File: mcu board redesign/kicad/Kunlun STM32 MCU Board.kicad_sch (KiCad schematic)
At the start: 33 parts, among them J1 0532610671, J2 10129383-908001ALF, J3 USB4105-GF-A, J4 5002, J5 5002, J6 5002, J7 5002, J8 5001, J9 5001, SW1 KMR231NG ULC LFS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

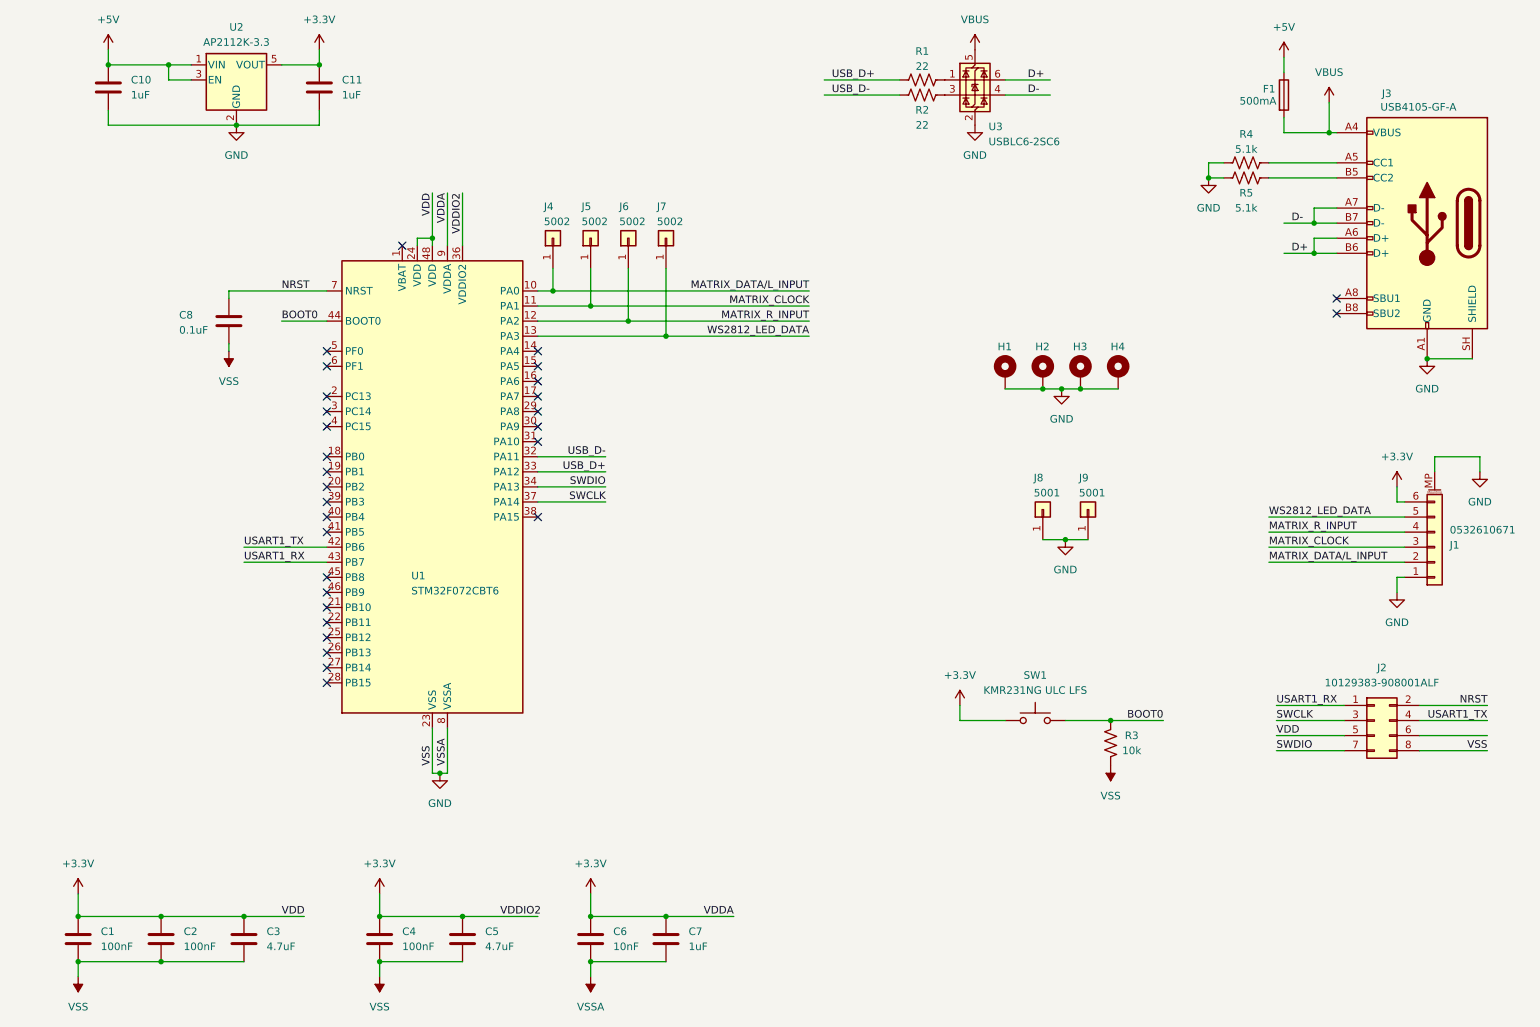
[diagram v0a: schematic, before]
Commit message: Lots of updates
Add ESD protection R6/C9
Layout changes for bypass caps
Layout changes to pass all JLC DFM checks
Fill out J2 and optimize routing
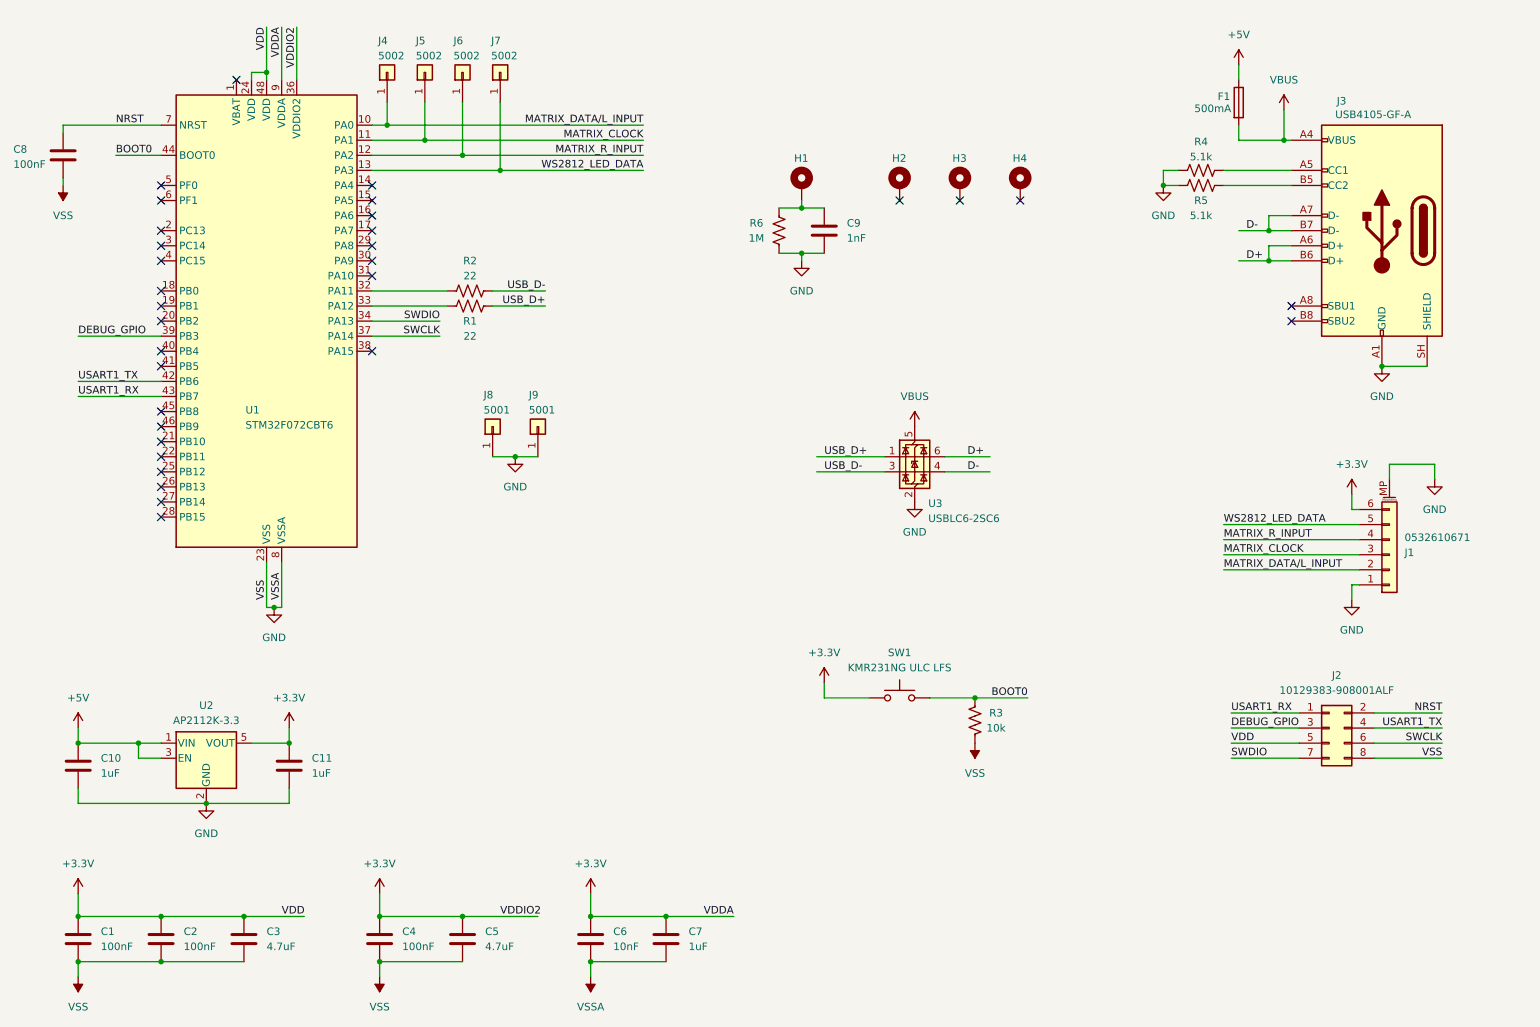
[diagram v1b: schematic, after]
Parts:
- added C9: 1nF, Capacitor_SMD:C_1206_3216Metric, symbol Device:C
- added R6: 1M, Resistor_SMD:R_1206_3216Metric, symbol Device:R_US
- C1, C2, C4: PartNo C0603C104K5RACTU -> 399-C0603C104K5RACTUCT-ND
- C10, C11, C7: PartNo C0603C105K4RACTU -> 399-C0603C105K4RACTUCT-ND
- C3, C5: PartNo (none) -> 399-C0603C475K9PACTUCT-ND
- C6: PartNo C0603C103K5RACTU -> 399-C0603C103K5RACTUCT-ND
- C8: value 0.1uF -> 100nF; PartNo C0603C104K5RACTU -> 399-C0603C104K5RACTUCT-ND
- H1, H2, H3, H4: footprint MountingHole:MountingHole_2.2mm_M2_Pad_Via -> MountingHole:MountingHole_2.2mm_M2_Pad
- J1: PartNo 0532610671 -> WM7624CT-ND
- J2: PartNo 10129383-908001ALF -> 609-10129383-908001ALFCT-ND
- J3: PartNo USB4105-GF-A -> 2073-USB4105-GF-ACT-ND
- J4, J5, J6, J7: PartNo (none) -> 36-5002-ND
- J8, J9: PartNo (none) -> 36-5001-ND
- R1, R2: PartNo RMCF0603FT22R0 -> RMCF0603FT22R0CT-ND
- R3: PartNo RMCF0603JT10K0 -> RMCF0603JT10K0CT-ND
- R4, R5: PartNo RC0603FR-075K1L -> RMCF0603FT5K10CT-ND
- SW1: PartNo KMR231NG ULC LFS -> CKN10284CT-ND
- U1: PartNo (none) -> 497-14645-ND
- U2: PartNo AP2112K-3.3 -> AP2112K-3.3TRG1DICT-ND
- U3: PartNo USBLC6-2SC6 -> 497-5235-1-ND
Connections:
- net GND: now also C9.2, R6.2; no longer H1.1, H2.1, H3.1, H4.1
- net SWCLK: now also J2.6 (Pin_6); no longer J2.3 (Pin_3)
- net USB_D+: now also R1.1, U3.1 (I/O1); no longer R1.2, U1.33 (PA12)
- net USB_D-: now also R2.1, U3.3 (I/O2); no longer R2.2, U1.32 (PA11)
- net DEBUG_GPIO: now reaches U1.39 (PB3)
- net DEBUG_GPIO: now also J2.3 (Pin_3)
- new net: C9.1, H1.1, R6.1
- new net: R2.2, U1.32 (PA11)
- new net: R1.2, U1.33 (PA12)
- no-connect marks 30 -> 32
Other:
- moved on the sheet: C10, C11, C8, F1, H1, J1, J2, J3, J4, J5, J6, J7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

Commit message: Mostly layout updates
Add VBUS decoupling cap.
Rearrange traces for less ground plane chops and fewer vias.
Move some components around for trace optimization (boot switch, etc)
Tweak the decoupling caps
Remove pads from 3 mounting holes to avoid potential chassis ground loops
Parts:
- removed H2, H3, H4: MountingHole_Pad, MountingHole:MountingHole_2.2mm_M2_Pad, symbol Mechanical:MountingHole_Pad
- added C10: 1uF, Capacitor_SMD:C_0603_1608Metric, symbol Device:C
- renumbered C10 to C11, C11 to C12
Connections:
- net GND: now also C10.2; no longer J1.MP (MountPin)
- net VBUS: now also C10.1
- no-connect marks 32 -> 30
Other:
- moved on the sheet: C1, C2, C3, C4, C5, C6, C7, C9, H1, R6

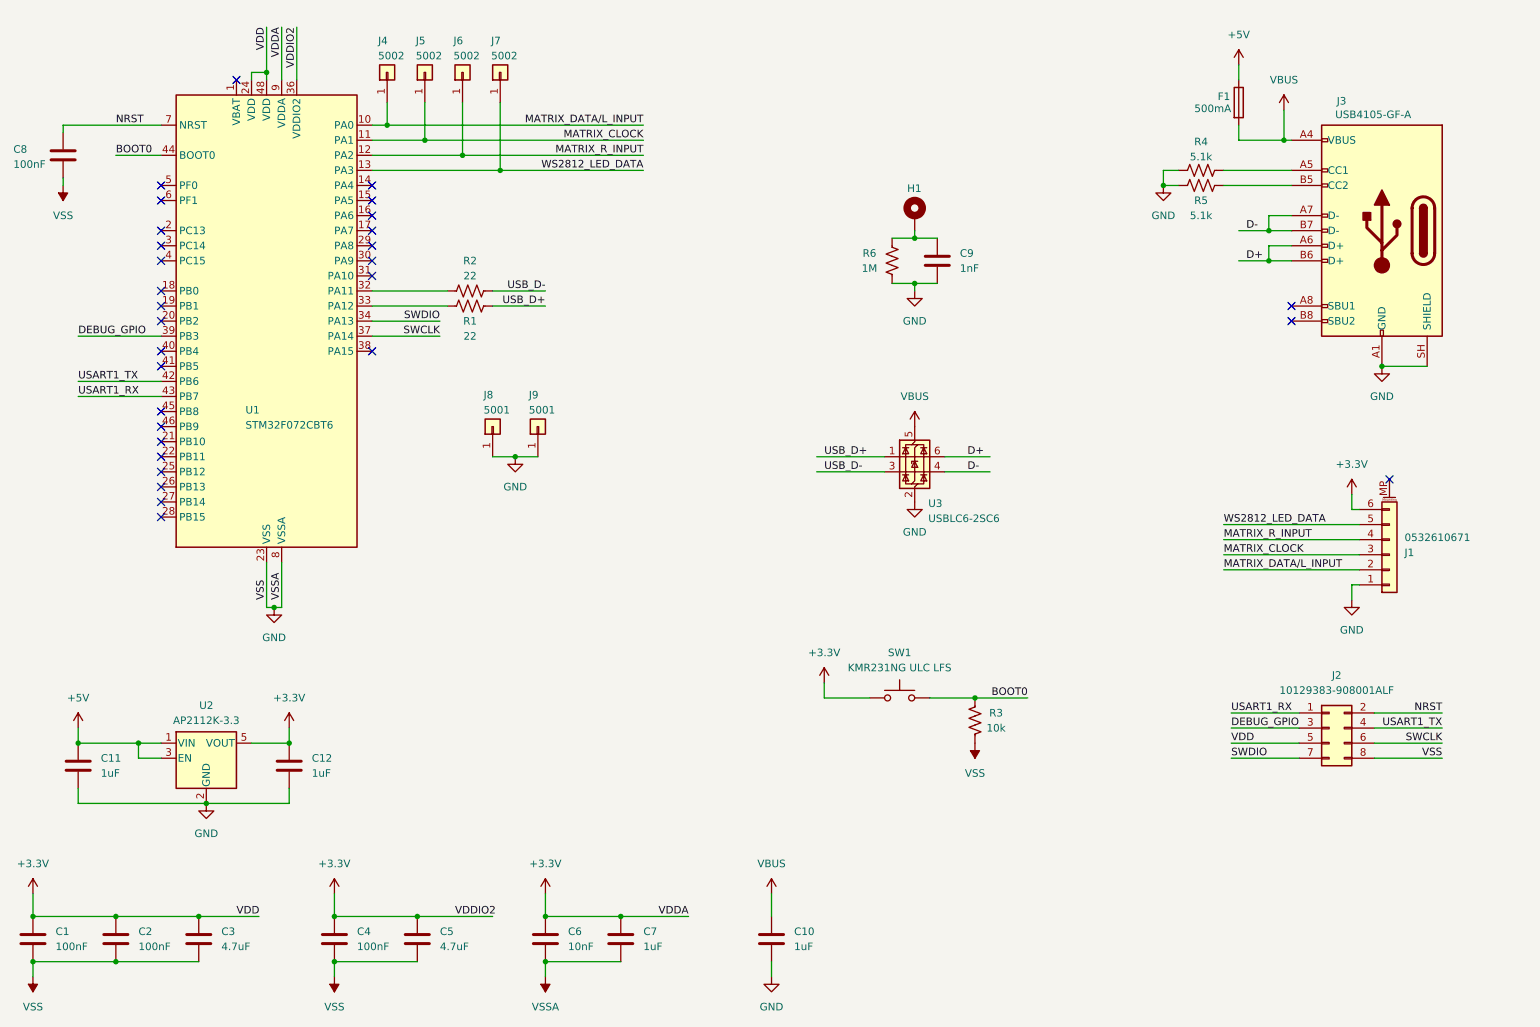
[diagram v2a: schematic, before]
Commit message: Added speaker, changed fuse.
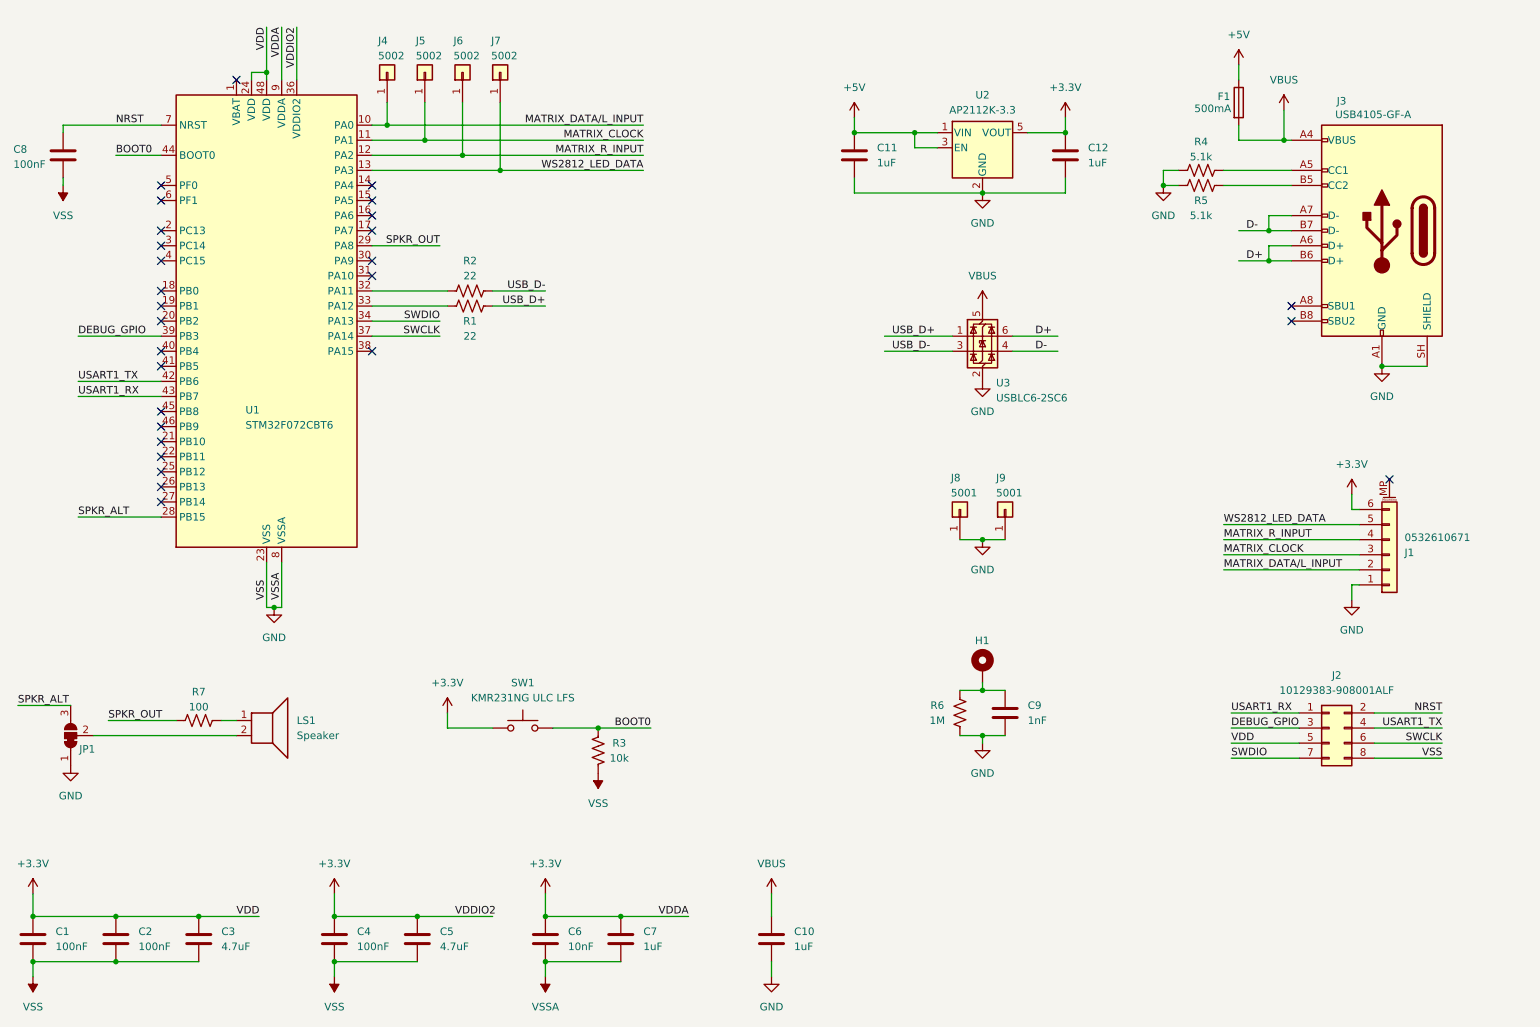
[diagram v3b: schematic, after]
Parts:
- added JP1: SolderJumper_3_Bridged12, Jumper:SolderJumper-3_P1.3mm_Bridged12_RoundedPad1.0x1.5mm, symbol Jumper:SolderJumper_3_Bridged12
- added LS1: Speaker, Buzzer_Beeper:Buzzer_CUI_CPT-9019S-SMT, symbol Device:Speaker
- added R7: 100, Resistor_SMD:R_0603_1608Metric, symbol Device:R_US
- F1: footprint Fuse:Fuse_1812_4532Metric -> Fuse:Fuse_1206_3216Metric; PartNo MF-MSMF050-2CT-ND -> 5923-0ZCJ0050FF2GCT-ND
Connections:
- net GND: now also JP1.1 (A)
- net SPKR_ALT: now reaches U1.28 (PB15)
- net SPKR_ALT: now also JP1.3 (B)
- net SPKR_OUT: now reaches U1.29 (PA8)
- net SPKR_OUT: now also R7.2
- new net: LS1.1, R7.1
- new net: JP1.2 (C), LS1.2
- no-connect marks 30 -> 28
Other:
- moved on the sheet: C11, C12, C9, H1, J8, J9, R3, R6, SW1, U2, U3

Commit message: Set correct PartNo for R7
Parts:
- R7: PartNo RMCF0603FT5K10CT-ND -> RMCF0603FT100RCT-ND
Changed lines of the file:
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@@
 			)
 		)
-		(property "PartNo" "RMCF0603FT5K10CT-ND"
+		(property "PartNo" "RMCF0603FT100RCT-ND"
 			(at 55.88 139.7 90)
 			(hide yes)

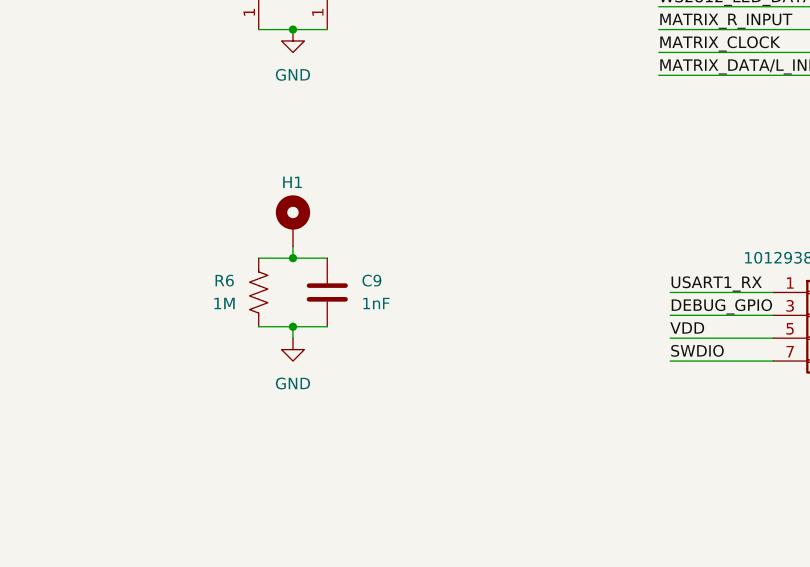
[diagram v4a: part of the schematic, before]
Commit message: Add a TVS to ESD circuit
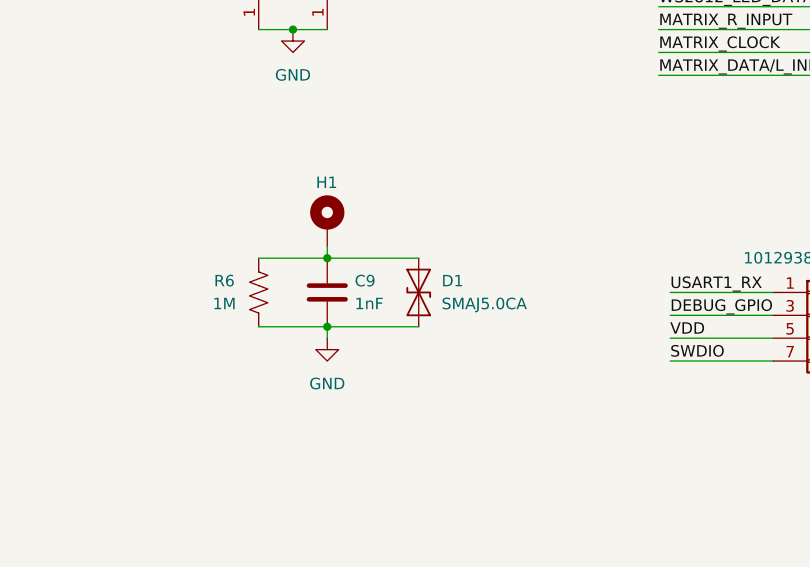
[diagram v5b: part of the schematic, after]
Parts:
- added D1: SMAJ5.0CA, Diode_SMD:D_SMA, symbol Diode:SMAJ5.0CA
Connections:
- net GND: now also D1.1 (A1)
- net at C9.1, H1.1, R6.1: now also D1.2 (A2)

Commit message: Add LCSC part numbers
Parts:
- C1, C2, C4, C8: Digikey (none) -> 399-C0603C104K5RACTUCT-ND; LCSC (none) -> C14663; PartNo 399-C0603C104K5RACTUCT-ND -> (none)
- C10, C11, C12, C7: Digikey (none) -> 399-C0603C105K4RACTUCT-ND; LCSC (none) -> C14663; PartNo 399-C0603C105K4RACTUCT-ND -> (none)
- C3, C5: Digikey (none) -> 399-C0603C475K9PACTUCT-ND; LCSC (none) -> C14663; PartNo 399-C0603C475K9PACTUCT-ND -> (none)
- C6: Digikey (none) -> 399-C0603C103K5RACTUCT-ND; LCSC (none) -> C57112; PartNo 399-C0603C103K5RACTUCT-ND -> (none)
- C9: Digikey (none) -> 311-1489-1-ND; LCSC (none) -> C9196; PartNo 311-1489-1-ND -> (none)
- D1: Digikey (none) -> SMAJ5.0CALFCT-ND; LCSC (none) -> C83324; PartNo SMAJ5.0CALFCT-ND -> (none)
- F1: Digikey (none) -> 5923-0ZCJ0050FF2GCT-ND; LCSC (none) -> C6964264; PartNo 5923-0ZCJ0050FF2GCT-ND -> (none)
- J1: Digikey (none) -> WM7624CT-ND; LCSC (none) -> C225115; PartNo WM7624CT-ND -> (none)
- J2: Digikey (none) -> 609-10129383-908001ALFCT-ND; LCSC (none) -> C49326142; PartNo 609-10129383-908001ALFCT-ND -> (none)
- J3: Digikey (none) -> 2073-USB4105-GF-ACT-ND; LCSC (none) -> C3020560; PartNo 2073-USB4105-GF-ACT-ND -> (none)
- J4, J5, J6, J7: Digikey (none) -> 36-5002-ND; LCSC (none) -> C238123; PartNo 36-5002-ND -> (none)
- J8, J9: Digikey (none) -> 36-5001-ND; LCSC (none) -> C238122; PartNo 36-5001-ND -> (none)
- LS1: Digikey (none) -> 102-3761-1-ND; LCSC (none) -> C95163; PartNo 102-3761-1-ND -> (none)
- R1, R2: Digikey (none) -> RMCF0603FT22R0CT-ND; LCSC (none) -> C23345; PartNo RMCF0603FT22R0CT-ND -> (none)
- R3: Digikey (none) -> RMCF0603JT10K0CT-ND; LCSC (none) -> C25804; PartNo RMCF0603JT10K0CT-ND -> (none)
- R4, R5: Digikey (none) -> RMCF0603FT5K10CT-ND; LCSC (none) -> C23186; PartNo RMCF0603FT5K10CT-ND -> (none)
- R6: Digikey (none) -> RMCF1206FT1M00CT-ND; LCSC (none) -> C17927; PartNo RMCF1206FT1M00CT-ND -> (none)
- R7: Digikey (none) -> RMCF0603FT100RCT-ND; LCSC (none) -> C2479061; PartNo RMCF0603FT100RCT-ND -> (none)
- SW1: Digikey (none) -> CKN10284CT-ND; LCSC (none) -> C99271; PartNo CKN10284CT-ND -> (none)
- U1: Digikey (none) -> 497-14645-ND; LCSC (none) -> C81720; PartNo 497-14645-ND -> (none)
- U2: Digikey (none) -> AP2112K-3.3TRG1DICT-ND; LCSC (none) -> C51118; PartNo AP2112K-3.3TRG1DICT-ND -> (none)
- U3: Digikey (none) -> 497-5235-1-ND; LCSC (none) -> C7519; PartNo 497-5235-1-ND -> (none)

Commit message: Update part numbers
Found alternates in LCSC that are "basic" instead of "extended" so manufacturing is considerably less expensive (saved $30 in setup costs).

Digikey is out of the AP2112 so list the AP7365 as an alternate.
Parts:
- C3, C5: Digikey 399-C0603C475K9PACTUCT-ND -> 1276-2087-1-ND
- U2: DigikeyAlt (none) -> AP7365-33WG-7DICT-ND
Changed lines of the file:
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@@
 			)
 		)
-		(property "PartNo" ""
+		(property "DigikeyAlt" "AP7365-33WG-7DICT-ND"
 			(at 187.96 43.18 0)
 			(hide yes)
@@
 			)
 		)
-		(property "Digikey" "399-C0603C475K9PACTUCT-ND"
+		(property "Digikey" "1276-2087-1-ND"
 			(at 92.71 176.53 0)
 			(hide yes)
@@
 			)
 		)
-		(property "Digikey" "399-C0603C475K9PACTUCT-ND"
+		(property "Digikey" "1276-2087-1-ND"
 			(at 55.88 176.53 0)
 			(hide yes)
